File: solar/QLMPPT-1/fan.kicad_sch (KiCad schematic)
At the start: 0 parts

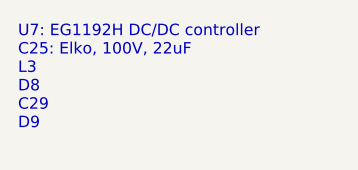
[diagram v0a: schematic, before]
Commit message: Sketching boost converter
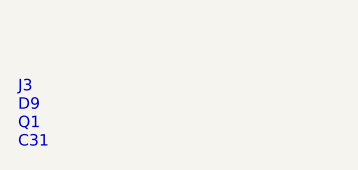
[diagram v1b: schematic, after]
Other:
- note added: "J3 D9 Q1 C31"
- note removed: "U7: EG1192H DC/DC controller C25: Elko, 100V, 22uF L3 D8 C29 D9"
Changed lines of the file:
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@@
 (kicad_sch (version 20211123) (generator eeschema)
   (paper "A4")
-  (text "U7: EG1192H DC/DC controller\nC25: Elko, 100V, 22uF\nL3\nD8\nC29\nD9\n\n"
-    (at 126.365 86.36 0)
+  (text "J3\nD9\nQ1\nC31\n" (at 126.365 86.36 0)
     (effects (font (size 1.27 1.27)) (justify left bottom))
   )
